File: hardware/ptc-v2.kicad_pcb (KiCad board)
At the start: 2 copper layers, 35 x 30 mm, 37 parts, among them J1 AKL_5_2, J2 AKL_5_2, P1 CON-SENSOR, P2 Debug, P3 Boot, P4 CONN_02X04, P5 CONN_02X04, U1 XMC1100, U2 MAX31865, U3 DRILL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

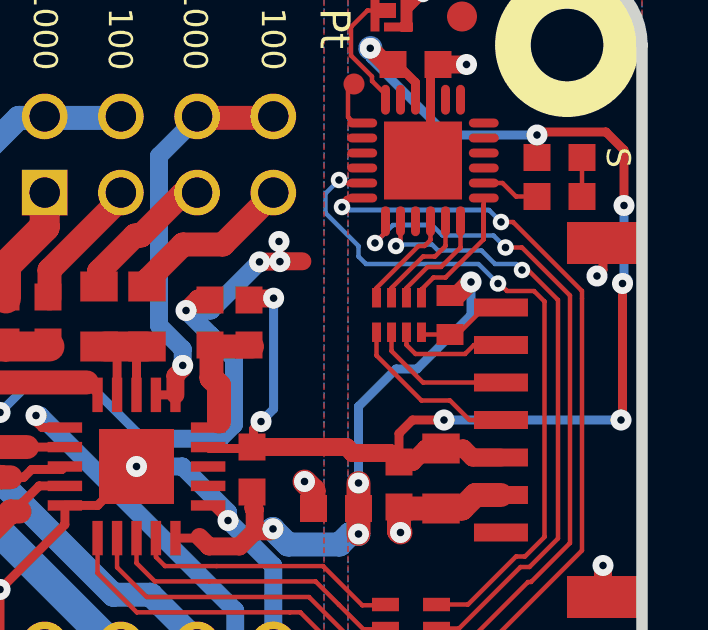
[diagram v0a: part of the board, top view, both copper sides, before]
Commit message: Change capacitor footprint(s) to C0402F
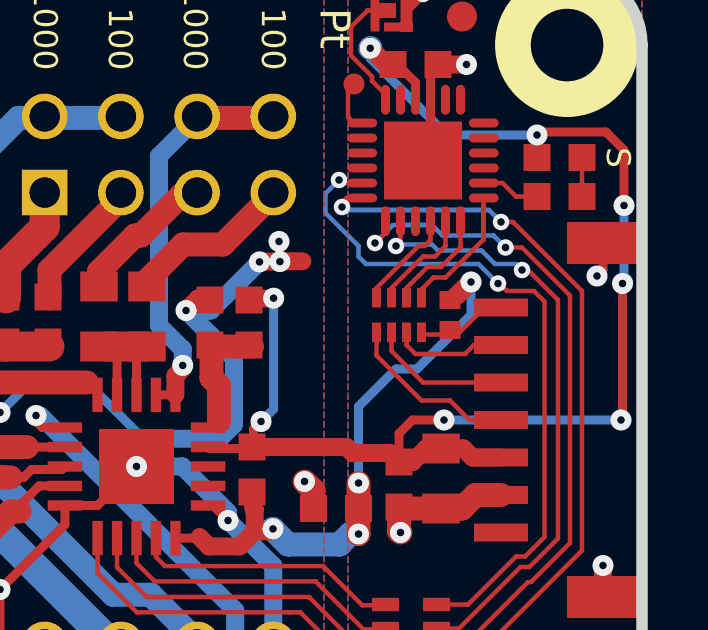
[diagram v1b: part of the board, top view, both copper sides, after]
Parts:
- C1: footprint C0402E -> kicad-libraries:C0402F
- C2: footprint C0805 -> kicad-libraries:C0805
- C3, C4, C5, C6, C7, C8: footprint C0603F -> kicad-libraries:C0603F
- D1: footprint D0603F -> kicad-libraries:D0603F
- FB1, FB2, R1: footprint R0603F -> kicad-libraries:R0603F
- J1, J2: footprint AKL_5_2 -> kicad-libraries:AKL_5_2
- P1: footprint CON-SENSOR2 -> kicad-libraries:CON-SENSOR2
- R2, R3: footprint R0805 -> kicad-libraries:R0805
- RP2: footprint 0603X4 -> kicad-libraries:0603X4
- U2: footprint QFN-20-5x5 -> kicad-libraries:QFN-20-5x5
- U3, U4, U5, U6: footprint DRILL_NP -> kicad-libraries:DRILL_NP
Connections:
- P1 pad 1: (no net) -> Net-(P1-Pad1)
- R2 pad 1: Net-(P4-Pad7) -> Net-(R2-Pad1)
- R3 pad 1: Net-(P4-Pad5) -> Net-(R3-Pad1)
- U1 pad 11: (no net) -> Net-(U1-Pad11)
- U1 pad 14: (no net) -> Net-(U1-Pad14)
- U1 pad 15: (no net) -> Net-(U1-Pad15)
- U1 pad 16: (no net) -> Net-(U1-Pad16)
- U1 pad 21: (no net) -> Net-(U1-Pad21)
- U1 pad 3: (no net) -> Net-(U1-Pad3)
- U1 pad 4: (no net) -> Net-(U1-Pad4)
- U1 pad 5: (no net) -> Net-(U1-Pad5)
- U1 pad 6: (no net) -> Net-(U1-Pad6)
- U1 pad 7: (no net) -> Net-(U1-Pad7)
- U1 pad 8: (no net) -> Net-(U1-Pad8)
- U2 pad 1: Net-(P4-Pad6) -> Net-(U2-Pad1)
- U2 pad 17: (no net) -> Net-(U2-Pad17)
- U2 pad 18: (no net) -> Net-(U2-Pad18)
- U2 pad 2: Net-(P4-Pad6) -> Net-(U2-Pad1)
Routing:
- net Net-(P4-Pad6): track 13.4 -> 11.1 mm, vias 1 -> 0
- net Net-(U2-Pad1): track 0.00 -> 2.27 mm, vias 0 -> 1
- net Net-(R3-Pad1): track 0.00 -> 2.20 mm
- net Net-(P4-Pad5): track 4.84 -> 2.64 mm
- net Net-(R2-Pad1): track 0.00 -> 1.90 mm
- net Net-(P4-Pad7): track 5.60 -> 3.71 mm

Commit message: fix netlist
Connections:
- P1 pad 1: Net-(P1-Pad1) -> (no net)
- R2 pad 1: Net-(R2-Pad1) -> Net-(P4-Pad7)
- R3 pad 1: Net-(R3-Pad1) -> Net-(P4-Pad5)
- U1 pad 11: Net-(U1-Pad11) -> (no net)
- U1 pad 14: Net-(U1-Pad14) -> (no net)
- U1 pad 15: Net-(U1-Pad15) -> (no net)
- U1 pad 16: Net-(U1-Pad16) -> (no net)
- U1 pad 21: Net-(U1-Pad21) -> (no net)
- U1 pad 3: Net-(U1-Pad3) -> (no net)
- U1 pad 4: Net-(U1-Pad4) -> (no net)
- U1 pad 5: Net-(U1-Pad5) -> (no net)
- U1 pad 6: Net-(U1-Pad6) -> (no net)
- U1 pad 7: Net-(U1-Pad7) -> (no net)
- U1 pad 8: Net-(U1-Pad8) -> (no net)
- U2 pad 1: Net-(U2-Pad1) -> Net-(P4-Pad6)
- U2 pad 17: Net-(U2-Pad17) -> (no net)
- U2 pad 18: Net-(U2-Pad18) -> (no net)
- U2 pad 2: Net-(U2-Pad1) -> Net-(P4-Pad6)
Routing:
- net Net-(P4-Pad6): track 11.1 -> 13.4 mm, vias 0 -> 1
- net Net-(U2-Pad1): track 2.27 -> 0.00 mm, vias 1 -> 0
- net Net-(R3-Pad1): track 2.20 -> 0.00 mm
- net Net-(P4-Pad5): track 2.64 -> 4.84 mm
- net Net-(R2-Pad1): track 1.90 -> 0.00 mm
- net Net-(P4-Pad7): track 3.71 -> 5.60 mm
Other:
- net class Default: clearance 0.15 -> 0.14
- rule trace_clearance: 0.15 -> 0.14

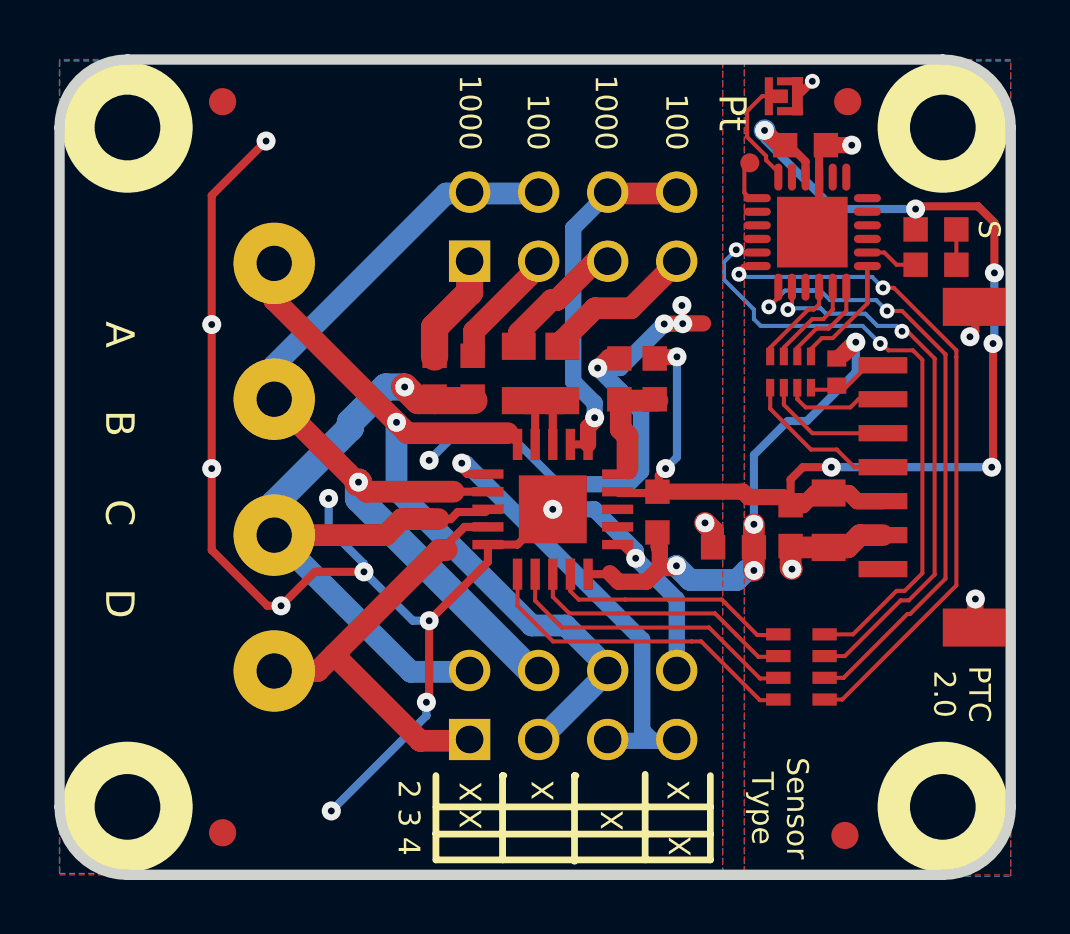
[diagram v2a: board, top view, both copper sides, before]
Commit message: fix resitor footprints, drc
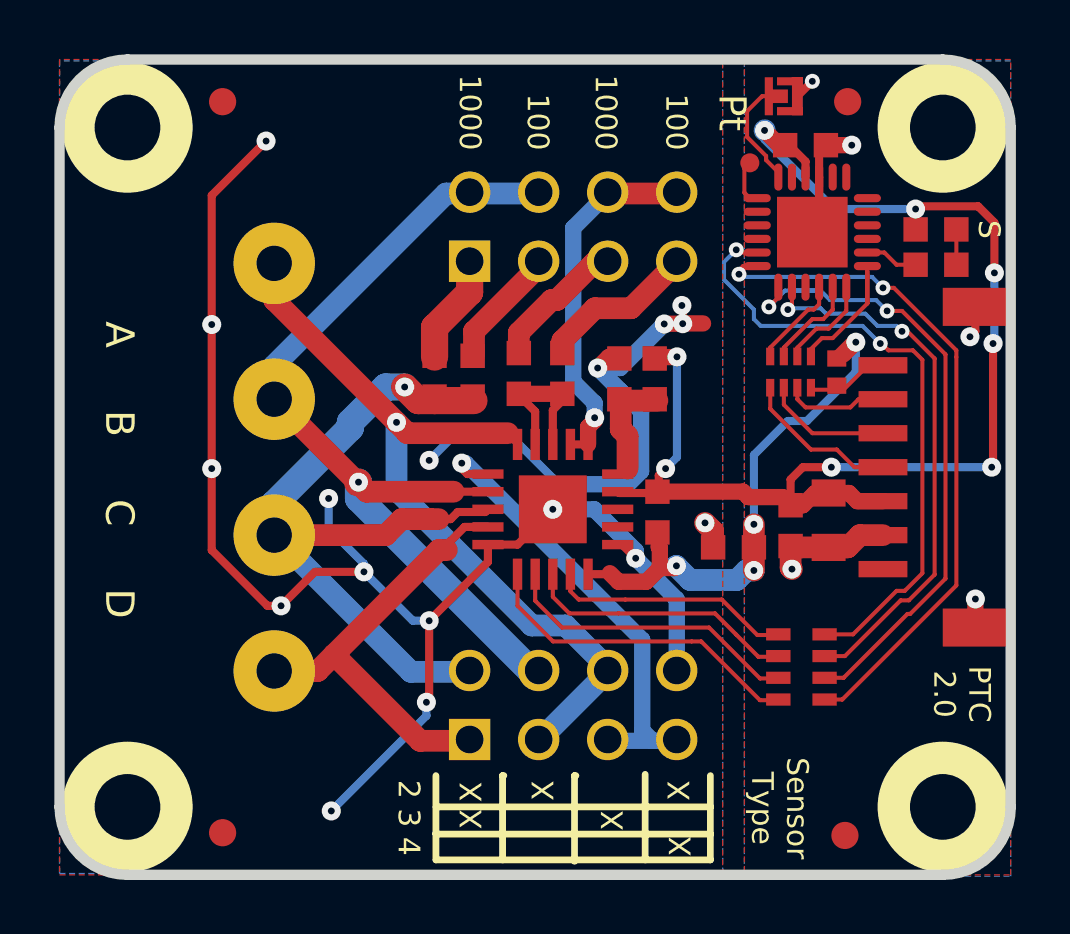
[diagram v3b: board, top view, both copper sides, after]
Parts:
- R2, R3: footprint kicad-libraries:R0805 -> kicad-libraries:R0603F
